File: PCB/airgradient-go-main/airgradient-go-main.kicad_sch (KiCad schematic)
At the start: 155 parts, among them CN1 SM02B-SRSS-TB (LF)(SN), CN2 BM05B-SRSS-TB(LF)(SN), CN3 BM05B-SRSS-TB(LF)(SN), CN4 HCZZ0039-4, Q1 SIA445EDJ-T1-GE3, Q2 ZVN4106FTA_C508255, Q3 SS8050-G, Q4 SI1308EDL, SW1 TS-1091C-A1B3-D2, SW2 TS-1091C-A1B3-D2, U1 W25N512GVEIG, U10 TMUX121NKGR_C22428404, U11 LIS2DH12TR, U12 HYG-8503A, U13 SHT4x, U14 ZDSD512MLGEAG, U15 DPS368XTSA1, U16 TAU1113, U17 S12, U18 TCA9536DTMR, U2 TPS63802DLAR, U3 BQ25628RYKR, U4 ESP32-C5-MINI-1, U5 TPL5010DDCR, U7 TPS7A0228DQNR, U8 BQ27427YZFR, U9 SGP41-D-R4

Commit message: Import v2.0 development state from Bitbucket branch v2.0
Overlay of the v2.0 design work onto the restructured PCB/ layout:
- airgradient-go-main v2.0 WIP: 186 footprints, microSD, PS1-CO,
  Birdy schematic review fixes; adds v2.0 BOM CSVs
- touch-pad v2.0: T1-T3 pads wired to touch controller CS channels,
  +3.1V rail renamed to VCC
- scd4x-module: minor updates
- libraries: new parts (SPL07-003, BM05B-SRSS-TB, PS1-CO, battery
  holder, ESP32-C5 models) and updated footprints; all library and
  3D model references normalized to ${KIPRJMOD}-relative paths
- led_pcb board was dropped in v2.0 (never migrated)

Known open items carried over from review: U14 VDD_IO not yet
connected to the 3.1V rail; U19 (LM66200) still fitted.
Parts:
- removed ANT1: GPS1003, easyeda2kicad:ANT-SMD_L10.0-W3.0, symbol easyeda2kicad:GPS1003
- removed C26, C38: 1uF/50V, easyeda2kicad:C0402, symbol easyeda2kicad:CC0402KRX5R9BB105
- removed C28: 2.2uF/16V, easyeda2kicad:C0402, symbol easyeda2kicad:CL05A225KO5NQNC
- removed CN1: SM02B-SRSS-TB (LF)(SN), easyeda2kicad:CONN-SMD_2P-P1.00_SM02B-SRSS-TB-LF-SN, symbol easyeda2kicad:SM02B-SRSS-TB(LF)(SN)
- removed CN2, CN3: BM05B-SRSS-TB(LF)(SN), easyeda2kicad:CONN-SMD-5P-P1.00_BM05B-SRSS-TB-LF-SN, symbol easyeda2kicad:BM05B-SRSS-TB(LF)(SN)
- removed CN4: HCZZ0039-4, easyeda2kicad:CONN-SMD_HCZZ0039-4, symbol easyeda2kicad:HCZZ0039-4
- removed D4, D5, D6, D7: CUS10S30,H3F, easyeda2kicad:SOD-323_L1.8-W1.3-LS2.5-RD, symbol easyeda2kicad:CUS10S30,H3F
- removed R28, R30: 10K, easyeda2kicad:R0402, symbol easyeda2kicad:MR04X1002FTL
- removed R29: 0R, easyeda2kicad:R0402, symbol easyeda2kicad:RC0402FR-070RL
- removed TP11: V1.8, TestPoint:TestPoint_Pad_D1.0mm, symbol Connector:TestPoint
- removed TP9: EN_PM1, TestPoint:TestPoint_Pad_D1.0mm, symbol Connector:TestPoint
- removed U15: DPS368XTSA1, easyeda2kicad:LGA-8_L2.5-W2.0-P0.65-TR_DPS368, symbol easyeda2kicad:DPS368XTSA1
- removed U18: TCA9536DTMR, easyeda2kicad:X2SON-8_L1.4-W0.8-P0.50-BL, symbol easyeda2kicad:TCA9536DTMR
- removed U8: BQ27427YZFR, easyeda2kicad:DSBGA-9_L1.6-W1.6-R3-C3-P0.50-TL, symbol easyeda2kicad:BQ27427YZFR
- added AE1: Antenna, AG-lib-oaf:CA-G01, symbol Device:Antenna
- added BT1: Battery_Cell, AG-lib-oaf:AGGO-battery, symbol Device:Battery_Cell
- added C10, C13, C16, C5, C7, C70, C71, C72, C73, C74, C9: 0.1uF/25V, Capacitor_SMD:C_0402_1005Metric, symbol Device:C
- added C26, C42, C66, C67, C68: 1uF/50V, Capacitor_SMD:C_0402_1005Metric, symbol Device:C
- added C27: 0.47uF/25V, Capacitor_SMD:C_0402_1005Metric, symbol Device:C
- added C69: 0.1uF/16V, Capacitor_SMD:C_0402_1005Metric, symbol Device:C
- added CN3, CN4, CN5: SM05B-SRSS-TB (LF)(SN), easyeda2kicad-oaf:CONN-SMD_SM05B-SRSS-TB-LF-SN, symbol easyeda2kicad-oaf:SM05B-SRSS-TB(LF)(SN)
- added LED1, LED2, LED3, LED4: TJ-S1608SW6TDSLCCYRGB-A5, easyeda2kicad-oaf:LED-ARRAY-SMD_4P-L1.6-W0.8-BL-FD, symbol easyeda2kicad-oaf:TJ-S1608SW6TDSLCCYRGB-A5
- added NT1: NetTie_2, NetTie:NetTie-2_SMD_Pad0.5mm, symbol Device:NetTie_2
- added NTC2: NCP15XH103F03RC, easyeda2kicad-oaf:R0402, symbol easyeda2kicad-oaf:NCP15XH103F03RC
- added Q3: CSD83325L, easyeda2kicad-oaf:PICOSTAR-6_L2.2-W1.1-R2-C3-P0.65-BL, symbol easyeda2kicad-oaf:CSD83325L
- added R12, R5: 200R, Resistor_SMD:R_0402_1005Metric, symbol Device:R
- added R13: 2K, Resistor_SMD:R_0402_1005Metric, symbol Device:R
- added R17, R20: 1K, Resistor_SMD:R_0402_1005Metric, symbol Device:R
- added R35: 470mR, Resistor_SMD:R_0805_2012Metric, symbol Device:R
- added R38, R46, R59: 100K, Resistor_SMD:R_0402_1005Metric, symbol Device:R
- added R47, R48: 0R, Resistor_SMD:R_0402_1005Metric, symbol Device:R
- added R49: 5.1K, Resistor_SMD:R_0402_1005Metric, symbol Device:R
- added R50, R51, R52, R53: 22R, Resistor_SMD:R_0402_1005Metric, symbol Device:R
- added R54, R55, R56, R57, R58: 10K, Resistor_SMD:R_0402_1005Metric, symbol Device:R
- added R6, R9: 10R, Resistor_SMD:R_0402_1005Metric, symbol Device:R
- added R8: 5mR 1%/1W, Resistor_SMD:R_1206_3216Metric, symbol Device:R
- added TF1: TF-CARD XG8P H1.5, easyeda2kicad-oaf:TF-SMD_TF-CARD-XG8P-H1.5, symbol easyeda2kicad-oaf:TF-CARDXG8PH1.5
- added TP16, TP17: VBUS, TestPoint:TestPoint_Pad_D1.0mm, symbol Connector:TestPoint
- added U11: PS1-CO-SMOKE-10k, AG-lib-oaf:PS1-CO-SMOKE-10k, symbol AG_lib-oaf:PS1-CO-SMOKE-10k
- added U13: SPL07-003, easyeda2kicad-oaf:LGA-10_L2.0-W2.0-P0.50-BL, symbol easyeda2kicad-oaf:SPL07-003
- added U17: TCA6408ARGT, Package_DFN_QFN:VQFN-16-1EP_3x3mm_P0.5mm_EP1.45x1.45mm, symbol Interface_Expansion:TCA6408ARGT
- added U19: LM66200DRLR, easyeda2kicad-oaf:SOT-583-8_L2.1-W1.2-P0.50-LS1.6-BL, symbol easyeda2kicad-oaf:LM66200DRLR
- added U20: LP5036, Package_DFN_QFN:VQFN-46-1EP_5x6mm_P0.4mm_EP2.8x3.8mm, symbol Driver_LED:LP5036
- added U3: BQ27742YZFR-G1, easyeda2kicad-oaf:DSBGA-15_L2.6-W2.0-R5-C3-P0.50-BL, symbol easyeda2kicad-oaf:BQ27742YZFR-G1
- C1: footprint easyeda2kicad:C0402 -> Capacitor_SMD:C_0402_1005Metric; symbol easyeda2kicad:CL05A104KA5NNNC -> Device:C
- C11: renamed from C4; footprint easyeda2kicad:C0603 -> Capacitor_SMD:C_0603_1608Metric; symbol easyeda2kicad:CL10A106MA8NRNC -> Device:C
- C12: renamed from C5; footprint easyeda2kicad:C0805 -> Capacitor_SMD:C_0805_2012Metric; symbol easyeda2kicad:CL21A226MAYNNNE -> Device:C
- C14: renamed from C33; footprint easyeda2kicad:C0402 -> Capacitor_SMD:C_0402_1005Metric; symbol easyeda2kicad:CL05A104KA5NNNC -> Device:C; now not fitted; now left out of the parts list
- C15: renamed from C6; footprint easyeda2kicad:C0402 -> Capacitor_SMD:C_0402_1005Metric; symbol easyeda2kicad:CL05A104KA5NNNC -> Device:C
- C17: renamed from C7; value 10uF/10V -> 0.1uF/10V; footprint easyeda2kicad:C0402 -> Capacitor_SMD:C_0402_1005Metric; symbol easyeda2kicad:CL05A106MP5NUNC_C315248 -> Device:C
- C18: renamed from C48; footprint easyeda2kicad:C0402 -> Capacitor_SMD:C_0402_1005Metric; symbol easyeda2kicad:CC0402KRX5R9BB105 -> Device:C; now not fitted; now left out of the parts list
- C19: renamed from C9; footprint easyeda2kicad:C0402 -> Capacitor_SMD:C_0402_1005Metric; symbol easyeda2kicad:CC0402KRX5R9BB105 -> Device:C
- C2: footprint easyeda2kicad:C0402 -> Capacitor_SMD:C_0402_1005Metric; symbol easyeda2kicad:0402B473K250NT -> Device:C
- C20: footprint easyeda2kicad:C1206 -> Capacitor_SMD:C_1206_3216Metric; symbol easyeda2kicad:GRM31CR61E476ME44L -> Device:C
- C21: renamed from C10; value 10uF/10V -> 22uF/10V; footprint easyeda2kicad:C0402 -> Capacitor_SMD:C_0402_1005Metric; symbol easyeda2kicad:CL05A106MP5NUNC_C315248 -> Device:C
- C22: renamed from C11; footprint easyeda2kicad:C0603 -> Capacitor_SMD:C_0603_1608Metric; symbol easyeda2kicad:CL10A106MA8NRNC -> Device:C
- C23: renamed from C24; now left out of the parts list
- C24: renamed from C14; footprint easyeda2kicad:C0402 -> Capacitor_SMD:C_0402_1005Metric; symbol easyeda2kicad:CL05A104KA5NNNC -> Device:C
- C25: renamed from C18; now left out of the parts list
- C28: renamed from C29; footprint easyeda2kicad:C0402 -> Capacitor_SMD:C_0402_1005Metric; symbol easyeda2kicad:CL05A104KA5NNNC -> Device:C
- C29: renamed from C27; footprint easyeda2kicad:C0402 -> Capacitor_SMD:C_0402_1005Metric; symbol easyeda2kicad:CC0402KRX5R9BB105 -> Device:C
- C3: renamed from C12; footprint easyeda2kicad:C0402 -> Capacitor_SMD:C_0402_1005Metric; symbol easyeda2kicad:CL05A104KA5NNNC -> Device:C
- C30: renamed from C19; footprint easyeda2kicad:C0402 -> Capacitor_SMD:C_0402_1005Metric; symbol easyeda2kicad:CC0402KRX5R9BB105 -> Device:C
- C31: renamed from C21; footprint easyeda2kicad:C0402 -> Capacitor_SMD:C_0402_1005Metric; symbol easyeda2kicad:CC0402KRX7R9BB102 -> Device:C; now left out of the parts list
- C32: renamed from C22; footprint easyeda2kicad:C0402 -> Capacitor_SMD:C_0402_1005Metric; symbol easyeda2kicad:CC0402KRX7R9BB102 -> Device:C; now left out of the parts list
- C33: renamed from C23; footprint easyeda2kicad:C0603 -> Capacitor_SMD:C_0603_1608Metric; symbol easyeda2kicad:0603B501K500NT -> Device:C
- C34: renamed from C25; footprint easyeda2kicad:C0402 -> Capacitor_SMD:C_0402_1005Metric; symbol easyeda2kicad:CC0402KRX7R6BB103 -> Device:C; now left out of the parts list
- C35: renamed from C31; footprint easyeda2kicad:C0402 -> Capacitor_SMD:C_0402_1005Metric; symbol easyeda2kicad:CC0402KRX5R9BB105 -> Device:C
- C36: renamed from C8; footprint easyeda2kicad:C0805 -> Capacitor_SMD:C_0805_2012Metric; symbol easyeda2kicad:CL21A226MAYNNNE -> Device:C
- C37: renamed from C13; footprint easyeda2kicad:C0805 -> Capacitor_SMD:C_0805_2012Metric; symbol easyeda2kicad:CL21A226MAYNNNE -> Device:C
- C38: renamed from C17; footprint easyeda2kicad:C0805 -> Capacitor_SMD:C_0805_2012Metric; symbol easyeda2kicad:CL21A226MAYNNNE -> Device:C
- C39: renamed from C49; footprint easyeda2kicad:C0402 -> Capacitor_SMD:C_0402_1005Metric; symbol easyeda2kicad:CL05A104KA5NNNC -> Device:C
- C4: renamed from C3; footprint easyeda2kicad:C0603 -> Capacitor_SMD:C_0603_1608Metric; symbol easyeda2kicad:CL10A106MA8NRNC -> Device:C
- C40: renamed from C52; footprint easyeda2kicad:C0402 -> Capacitor_SMD:C_0402_1005Metric; symbol easyeda2kicad:CC0402KRX5R9BB105 -> Device:C
- C41: renamed from C34; footprint easyeda2kicad:C0402 -> Capacitor_SMD:C_0402_1005Metric; symbol easyeda2kicad:CC0402KRX5R9BB105 -> Device:C
- C43: renamed from C35; footprint easyeda2kicad:C0402 -> Capacitor_SMD:C_0402_1005Metric; symbol easyeda2kicad:CC0402KRX5R9BB105 -> Device:C
- C44: renamed from C39; footprint easyeda2kicad:C0402 -> Capacitor_SMD:C_0402_1005Metric; symbol easyeda2kicad:CC0402KRX5R9BB105 -> Device:C
- C45: renamed from C30; footprint easyeda2kicad:C0402 -> Capacitor_SMD:C_0402_1005Metric; symbol easyeda2kicad:CGA0402X5R475M250GT -> Device:C
- C46: renamed from C41; footprint easyeda2kicad:C0402 -> Capacitor_SMD:C_0402_1005Metric; symbol easyeda2kicad:CC0402KRX5R9BB105 -> Device:C
- C47: renamed from C56; footprint easyeda2kicad:C0402 -> Capacitor_SMD:C_0402_1005Metric; symbol easyeda2kicad:CC0402KRX5R9BB105 -> Device:C
- C48: renamed from C32; footprint easyeda2kicad:C0402 -> Capacitor_SMD:C_0402_1005Metric; symbol easyeda2kicad:CGA0402X5R475M250GT -> Device:C
- C49: renamed from C40; footprint easyeda2kicad:C0402 -> Capacitor_SMD:C_0402_1005Metric; symbol easyeda2kicad:CC0402KRX5R9BB105 -> Device:C
- C50: renamed from C57; footprint easyeda2kicad:C0402 -> Capacitor_SMD:C_0402_1005Metric; symbol easyeda2kicad:CC0402KRX5R9BB105 -> Device:C
- C51: renamed from C42; footprint easyeda2kicad:C0402 -> Capacitor_SMD:C_0402_1005Metric; symbol easyeda2kicad:CC0402KRX5R9BB105 -> Device:C
- C52: renamed from C58; footprint easyeda2kicad:C0402 -> Capacitor_SMD:C_0402_1005Metric; symbol easyeda2kicad:CL05A104KA5NNNC -> Device:C
- C53: renamed from C43; footprint easyeda2kicad:C0402 -> Capacitor_SMD:C_0402_1005Metric; symbol easyeda2kicad:CC0402KRX5R9BB105 -> Device:C
- C54: renamed from C36; footprint easyeda2kicad:C0402 -> Capacitor_SMD:C_0402_1005Metric; symbol easyeda2kicad:CC0402KRX5R9BB105 -> Device:C
- C55: renamed from C37; footprint easyeda2kicad:C0402 -> Capacitor_SMD:C_0402_1005Metric; symbol easyeda2kicad:CC0402KRX5R9BB105 -> Device:C
- C56: renamed from C50; footprint easyeda2kicad:C0402 -> Capacitor_SMD:C_0402_1005Metric; symbol easyeda2kicad:CL05A104KA5NNNC -> Device:C
- C57: renamed from C60; footprint easyeda2kicad:C0402 -> Capacitor_SMD:C_0402_1005Metric; symbol easyeda2kicad:CL05A104KA5NNNC -> Device:C
- C58: renamed from C45; footprint easyeda2kicad:C0402 -> Capacitor_SMD:C_0402_1005Metric; symbol easyeda2kicad:CC0402KRX5R9BB105 -> Device:C
- C59: renamed from C46; footprint easyeda2kicad:C0402 -> Capacitor_SMD:C_0402_1005Metric; symbol easyeda2kicad:CL05A104KA5NNNC -> Device:C
- C6: renamed from C15; footprint easyeda2kicad:C0603 -> Capacitor_SMD:C_0603_1608Metric; symbol easyeda2kicad:CL10A106MA8NRNC -> Device:C
- C60: renamed from C53; footprint easyeda2kicad:C0603 -> Capacitor_SMD:C_0603_1608Metric; symbol easyeda2kicad:CL10A106MA8NRNC -> Device:C
- C61: renamed from C47; now left out of the parts list
- C62: renamed from C51; now left out of the parts list
- C63: renamed from C54; footprint easyeda2kicad:C0402 -> Capacitor_SMD:C_0402_1005Metric; symbol easyeda2kicad:CL05A104KA5NNNC -> Device:C
- C64: renamed from C55; footprint easyeda2kicad:C0402 -> Capacitor_SMD:C_0402_1005Metric; symbol easyeda2kicad:CC0402KRX5R9BB105 -> Device:C
- C65: renamed from C59; footprint easyeda2kicad:C0603 -> Capacitor_SMD:C_0603_1608Metric; symbol easyeda2kicad:CL10A106MA8NRNC -> Device:C
- C8: renamed from C16; footprint easyeda2kicad:C0402 -> Capacitor_SMD:C_0402_1005Metric; symbol easyeda2kicad:CGA0402X5R475M250GT -> Device:C
- D3: renamed from D1; footprint easyeda2kicad:SOD-882_L1.0-W0.6-RD -> easyeda2kicad-oaf:SOD-882_L1.0-W0.6-RD; symbol easyeda2kicad:PMEG3005EL,315 -> easyeda2kicad-oaf:PMEG3005EL,315
- D4: renamed from D2; footprint easyeda2kicad:SOD-882_L1.0-W0.6-RD -> easyeda2kicad-oaf:SOD-882_L1.0-W0.6-RD; symbol easyeda2kicad:PMEG3005EL,315 -> easyeda2kicad-oaf:PMEG3005EL,315
- D5: renamed from D3; footprint easyeda2kicad:SOD-882_L1.0-W0.6-RD -> easyeda2kicad-oaf:SOD-882_L1.0-W0.6-RD; symbol easyeda2kicad:PMEG3005EL,315 -> easyeda2kicad-oaf:PMEG3005EL,315
- F1: footprint easyeda2kicad:F1206 -> easyeda2kicad-oaf:F1206; symbol easyeda2kicad:BSMD1206-075-6V -> easyeda2kicad-oaf:BSMD1206-075-6V
- FPC1: footprint easyeda2kicad:FPC-SMD_FPC-0.5-24P-LTH2.0 -> easyeda2kicad-oaf:FPC-SMD_FPC-0.5-24P-LTH2.0; symbol easyeda2kicad:FPC0.5-24PLTH2.0 -> easyeda2kicad-oaf:FPC0.5-24PLTH2.0
- L1: footprint easyeda2kicad:IND-SMD_L2.5-W2.0 -> easyeda2kicad-oaf:IND-SMD_L2.5-W2.0; symbol easyeda2kicad:252012CDMCDDS-1R0MC -> easyeda2kicad-oaf:252012CDMCDDS-1R0MC
- L2: footprint easyeda2kicad:IND-SMD_L4.0-W4.0_XGL4020 -> easyeda2kicad-oaf:IND-SMD_L4.0-W4.0_XGL4020; symbol easyeda2kicad:XGL4020-471MEC -> easyeda2kicad-oaf:XGL4020-471MEC
- L3: footprint easyeda2kicad:L0805 -> easyeda2kicad-oaf:L0805; symbol easyeda2kicad:XRTC201210S100MBCA -> easyeda2kicad-oaf:XRTC201210S100MBCA
- NTC1: footprint easyeda2kicad:R0805 -> easyeda2kicad-oaf:R0805; symbol easyeda2kicad:KNTC0805_10KF3950 -> easyeda2kicad-oaf:KNTC0805_10KF3950
- Q1: footprint easyeda2kicad:SC-70-6L_L2.0-W2.0-P0.65-BL -> easyeda2kicad-oaf:SC-70-6L_L2.0-W2.0-P0.65-BL; symbol easyeda2kicad:SIA445EDJ-T1-GE3 -> easyeda2kicad-oaf:SIA445EDJ-T1-GE3
- Q2: footprint easyeda2kicad:SOT-23-3_L2.9-W1.3-P1.90-LS2.4-BR -> easyeda2kicad-oaf:SOT-23-3_L2.9-W1.3-P1.90-LS2.4-BR; symbol easyeda2kicad:ZVN4106FTA_C508255 -> easyeda2kicad-oaf:ZVN4106FTA_C508255
- Q4: renamed from Q3; footprint easyeda2kicad:SOT-23-3_L2.9-W1.3-P1.90-LS2.4-BR -> easyeda2kicad-oaf:SOT-23-3_L2.9-W1.3-P1.90-LS2.4-BR; symbol easyeda2kicad:SS8050-G -> easyeda2kicad-oaf:SS8050-G
- Q5: renamed from Q4; footprint easyeda2kicad:SOT-323-3_L2.0-W1.3-P1.30-LS2.1-BR -> easyeda2kicad-oaf:SOT-323-3_L2.0-W1.3-P1.30-LS2.1-BR; symbol easyeda2kicad:SI1308EDL -> easyeda2kicad-oaf:SI1308EDL
- R1: footprint easyeda2kicad:R0402 -> Resistor_SMD:R_0402_1005Metric; symbol easyeda2kicad:RC0402FR-07100KL -> Device:R
- R10: renamed from R14; footprint easyeda2kicad:R0402 -> Resistor_SMD:R_0402_1005Metric; symbol easyeda2kicad:MR04X1002FTL -> Device:R
- R11: renamed from R9; footprint easyeda2kicad:R0402 -> Resistor_SMD:R_0402_1005Metric; symbol easyeda2kicad:RC0402FR-075K1L -> Device:R
- R14: renamed from R10; footprint easyeda2kicad:R0402 -> Resistor_SMD:R_0402_1005Metric; symbol easyeda2kicad:MR04X1002FTL -> Device:R
- R15: renamed from R17; footprint easyeda2kicad:R0402 -> Resistor_SMD:R_0402_1005Metric; symbol easyeda2kicad:0402WGF1502TCE -> Device:R
- R16: renamed from R18; footprint easyeda2kicad:R0402 -> Resistor_SMD:R_0402_1005Metric; symbol easyeda2kicad:RC0402FR-0720KL -> Device:R
- R18: renamed from R11; footprint easyeda2kicad:R0402 -> Resistor_SMD:R_0402_1005Metric; symbol easyeda2kicad:RC0402FR-074K12L -> Device:R
- R19: renamed from R12; footprint easyeda2kicad:R0402 -> Resistor_SMD:R_0402_1005Metric; symbol easyeda2kicad:AT0402DRD0717K4L -> Device:R
- R2, R3: footprint easyeda2kicad:R0402 -> Resistor_SMD:R_0402_1005Metric; symbol easyeda2kicad:MR04X1002FTL -> Device:R
- R21: renamed from R13; footprint easyeda2kicad:R0402 -> Resistor_SMD:R_0402_1005Metric; symbol easyeda2kicad:0402WGF2491TCE -> Device:R
- R22: renamed from R4; footprint easyeda2kicad:R0402 -> Resistor_SMD:R_0402_1005Metric; symbol easyeda2kicad:FRC0402F4753TS -> Device:R
- R23: renamed from R38; footprint easyeda2kicad:R0402 -> Resistor_SMD:R_0402_1005Metric; symbol easyeda2kicad:RC0402FR-071KL -> Device:R
- R24: renamed from R6; footprint easyeda2kicad:R0402 -> Resistor_SMD:R_0402_1005Metric; symbol easyeda2kicad:RC0402FR-0791KL -> Device:R
- R25: renamed from R16; footprint easyeda2kicad:R0402 -> Resistor_SMD:R_0402_1005Metric; symbol easyeda2kicad:RC0402FR-0751KL -> Device:R
- R26: renamed from R19; footprint easyeda2kicad:R0402 -> Resistor_SMD:R_0402_1005Metric; symbol easyeda2kicad:MR04X1002FTL -> Device:R
- R27: renamed from R20; footprint easyeda2kicad:R0402 -> Resistor_SMD:R_0402_1005Metric; symbol easyeda2kicad:RC0402FR-0722RL -> Device:R
- R28: renamed from R21; footprint easyeda2kicad:R0402 -> Resistor_SMD:R_0402_1005Metric; symbol easyeda2kicad:RC0402FR-0722RL -> Device:R
- R29: renamed from R8; footprint easyeda2kicad:R0402 -> Resistor_SMD:R_0402_1005Metric; symbol easyeda2kicad:RC0402FR-07100KL -> Device:R
- R30: renamed from R22; footprint easyeda2kicad:R0402 -> Resistor_SMD:R_0402_1005Metric; symbol easyeda2kicad:MR04X1002FTL -> Device:R
- R31: renamed from R23; footprint easyeda2kicad:R0402 -> Resistor_SMD:R_0402_1005Metric; symbol easyeda2kicad:RC0402FR-07100KL -> Device:R
- R32: renamed from R25; value 0R -> 50mR; footprint easyeda2kicad:R0402 -> Resistor_SMD:R_0805_2012Metric; symbol easyeda2kicad:RC0402FR-070RL -> Device:R
- R33: renamed from R24; value 10K -> 100K; footprint easyeda2kicad:R0402 -> Resistor_SMD:R_0402_1005Metric; symbol easyeda2kicad:MR04X1002FTL -> Device:R
- R34: renamed from R36; footprint easyeda2kicad:R0402 -> Resistor_SMD:R_0402_1005Metric; symbol easyeda2kicad:MR04X1002FTL -> Device:R; now not fitted; now left out of the parts list
- R36: renamed from R26; footprint easyeda2kicad:R0402 -> Resistor_SMD:R_0402_1005Metric; symbol easyeda2kicad:MR04X1002FTL -> Device:R
- R37: renamed from R27; footprint easyeda2kicad:R0402 -> Resistor_SMD:R_0402_1005Metric; symbol easyeda2kicad:MR04X1002FTL -> Device:R; now not fitted
- R39: renamed from R31; footprint easyeda2kicad:R0402 -> Resistor_SMD:R_0402_1005Metric; symbol easyeda2kicad:RC0402FR-07100KL -> Device:R
- R4: renamed from R5; footprint easyeda2kicad:R0402 -> Resistor_SMD:R_0402_1005Metric; symbol easyeda2kicad:RC0402FR-07100KL -> Device:R
- R40: renamed from R33; footprint easyeda2kicad:R0402 -> Resistor_SMD:R_0402_1005Metric; symbol easyeda2kicad:RC0402FR-07100KL -> Device:R
- R41: renamed from R35; footprint easyeda2kicad:R0402 -> Resistor_SMD:R_0402_1005Metric; symbol easyeda2kicad:FRC0402F4R70TS -> Device:R
- R42: renamed from R32; footprint easyeda2kicad:R0402 -> Resistor_SMD:R_0402_1005Metric; symbol easyeda2kicad:RC0402FR-071ML -> Device:R
- R43: renamed from R34; footprint easyeda2kicad:R0402 -> Resistor_SMD:R_0402_1005Metric; symbol easyeda2kicad:0402WGF220KTCE -> Device:R
- R44: renamed from R37; value 10K -> 100K; footprint easyeda2kicad:R0402 -> Resistor_SMD:R_0402_1005Metric; symbol easyeda2kicad:MR04X1002FTL -> Device:R
- R45: renamed from R39; footprint easyeda2kicad:R0402 -> Resistor_SMD:R_0402_1005Metric; symbol easyeda2kicad:RC0402FR-070RL -> Device:R
- R7: footprint easyeda2kicad:R0402 -> Resistor_SMD:R_0402_1005Metric; symbol easyeda2kicad:RC0402FR-075K1L -> Device:R
- SW1, SW2: footprint easyeda2kicad:KEY-SMD_3P-L5.5-W3.8-P3.00 -> easyeda2kicad-oaf:KEY-SMD_3P-L5.5-W3.8-P3.00; symbol easyeda2kicad:TS-1091C-A1B3-D2 -> easyeda2kicad-oaf:TS-1091C-A1B3-D2
- TP1: renamed from TP3; now not fitted; now left out of the parts list
- TP10: renamed from TP13; now not fitted; now left out of the parts list
- TP11: renamed from TP14; now not fitted; now left out of the parts list
- TP12: renamed from TP15; now not fitted; now left out of the parts list
- TP13: renamed from TP16; now not fitted; now left out of the parts list
- TP14: renamed from TP17; now not fitted; now left out of the parts list
- TP15: renamed from TP18; now not fitted; now left out of the parts list
- TP2: renamed from TP4; now not fitted; now left out of the parts list
- TP3: renamed from TP1; now not fitted; now left out of the parts list
- TP4: renamed from TP6; now not fitted; now left out of the parts list
- TP5: renamed from TP8; now not fitted; now left out of the parts list
- TP6: renamed from TP7; now not fitted; now left out of the parts list
- TP7: renamed from TP10; now not fitted; now left out of the parts list
- TP8: renamed from TP5; now not fitted; now left out of the parts list
- U1: footprint easyeda2kicad:WSON-8_L8.0-W6.0-P1.27-TL-1 -> easyeda2kicad-oaf:WSON-8_L8.0-W6.0-P1.27-TL-1; symbol easyeda2kicad:W25N512GVEIG -> easyeda2kicad-oaf:W25N512GVEIG
- U10: renamed from U9; footprint Senserion:XDCR_SGP41-D-R4 -> Senserion-oaf:XDCR_SGP41-D-R4; symbol Senserion:SGP41-D-R4 -> Senserion-oaf:SGP41-D-R4; now left out of the parts list
- U12: renamed from U13; now left out of the parts list
- U14: renamed from U11; footprint easyeda2kicad:LGA-12_L2.0-W2.0-P0.50-BL -> easyeda2kicad-oaf:LGA-12_L2.0-W2.0-P0.50-BL; symbol easyeda2kicad:LIS2DH12TR -> easyeda2kicad-oaf:LIS2DH12TR
- U15: renamed from U10; footprint easyeda2kicad:UQFN-10_L1.8-W1.4-P0.40-BL -> easyeda2kicad-oaf:UQFN-10_L1.8-W1.4-P0.40-BL; symbol easyeda2kicad:TMUX121NKGR_C22428404 -> easyeda2kicad-oaf:TMUX121NKGR_C22428404
- U16: renamed from U17; footprint S12:S12 -> S12-oaf:S12; symbol S12:S12 -> S12-oaf:S12; now left out of the parts list
- U18: renamed from U16; footprint RF_GPS:TAU1113 -> RF_GPS-oaf:TAU1113; symbol RF_GPS:TAU1113 -> RF_GPS-oaf:TAU1113
- U2: renamed from U14; footprint easyeda2kicad:LGA-8_L8.0-W6.0-P1.27-TL -> easyeda2kicad-oaf:LGA-8_L8.0-W6.0-P1.27-TL; symbol easyeda2kicad:ZDSD512MLGEAG -> easyeda2kicad-oaf:ZDSD512MLGEAG; now left out of the parts list
- U4: footprint Esparessif:ESP32-C5-MINI-1 -> Esparessif-oaf:ESP32-C5-MINI-1; symbol Espressif:ESP32-C5-MINI-1 -> Espressif-oaf:ESP32-C5-MINI-1; now left out of the parts list
- U5: renamed from U3; footprint easyeda2kicad:WQFN-18_L3.0-W2.5-P0.40-TL -> easyeda2kicad-oaf:WQFN-18_L3.0-W2.5-P0.40-TL; symbol easyeda2kicad:BQ25628RYKR -> easyeda2kicad-oaf:BQ25628RYKR
- U6: renamed from U12; footprint easyeda2kicad:BUZ-SMD_4P-L8.5-W8.5-P8.50-BR -> easyeda2kicad-oaf:BUZ-SMD_4P-L8.5-W8.5-P8.50-BR; symbol easyeda2kicad:HYG-8503A -> easyeda2kicad-oaf:HYG-8503A
- U7: renamed from U5; footprint easyeda2kicad:SOT-23-6_L2.9-W1.6-P0.95-LS2.8-BR -> easyeda2kicad-oaf:SOT-23-6_L2.9-W1.6-P0.95-LS2.8-BR; symbol easyeda2kicad:TPL5010DDCR -> easyeda2kicad-oaf:TPL5010DDCR
- U8: renamed from U2; footprint easyeda2kicad:VSON-10_L3.0-W2.0-P0.50-TL -> easyeda2kicad-oaf:VSON-10_L3.0-W2.0-P0.50-TL; symbol easyeda2kicad:TPS63802DLAR -> easyeda2kicad-oaf:TPS63802DLAR
- U9: renamed from U7; footprint easyeda2kicad:X2SON-4_L1.0-W1.0-P0.65-TL-EP -> easyeda2kicad-oaf:X2SON-4_L1.0-W1.0-P0.65-TL-EP; symbol easyeda2kicad:TPS7A0228DQNR -> easyeda2kicad-oaf:TPS7A0228DQNR
- USB1: footprint easyeda2kicad:USB-C-SMD_G-SWITCH_GT-USB-7010ASV -> easyeda2kicad-oaf:USB-C-SMD_G-SWITCH_GT-USB-7010ASV; symbol easyeda2kicad:GT-USB-7010ASV -> easyeda2kicad-oaf:GT-USB-7010ASV
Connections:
- net +3.1V: now also C42.2, C69.2, C70.2, C71.2, CN4.1, CN5.5, LED1.1 (+), LED2.1 (+), LED3.1 (+), LED4.1 (+), R38.2, R47.1, R54.2, R55.2, R56.2, R57.2, R58.2, R59.2, TF1.4 (VDD), U13.1 (VDDIO), U13.10 (VDD), U17.14 (V_{CCP}), U17.15 (V_{CCI}), U20.39 (ADDR1), U20.40 (VCC), U20.43 (EN); no longer R29.1, U14.10 (VDD_IO), U14.2 (CS)
- net +5V: now also CN3.1
- net ACC_INT: now also U17.8 (P5); no longer U4.7 (IO3)
- net EN_PM1: now also R38.1, U17.3 (P1); no longer R37.1, U4.34 (IO26)
- net GND: now also C42.1, C66.1, C67.1, C68.1, C69.1, C70.1, C71.1, C74.1, CN3.4, CN3.5, CN3.6, CN3.7, CN4.5, CN4.6, CN4.7, CN5.1, CN5.6, CN5.7, NT1.2, R48.1, R49.1, TF1.10 (GND), TF1.11 (GND), TF1.12 (GND), TF1.6 (VSS), TF1.9 (GND), U13.3 (GND), U13.8 (GND), U13.9 (GND), U17.16 (ADDR), U17.17 (EPAD), U17.6 (GND), U19.1 (GND), U19.4 (~{ON}), U19.5 (GND), U20.37 (GND), U20.46 (GND), U20.47 (GND)
- net INT: now also CN4.4, U17.7 (P4); no longer U4.17 (IO1)
- net MISO: now also R50.1
- net MOSI: now also R52.2
- net NAND CS: now also U17.4 (P2); no longer U4.8 (IO4)
- net PM_SCL: now also CN3.3
- net PM_SDA: now also CN3.2
- net PRTRG: now also U17.2 (P0)
- net SCL: now also CN4.3, CN5.3, U13.2 (SCL), U17.12 (SCL), U20.42 (SCL), U3.E3 (SCL)
- net SCLK: now also R51.1
- net SDA: now also CN4.2, CN5.4, U13.4 (SDA), U17.13 (SDA), U20.41 (SDA), U3.C3 (SDA)
- net SYS: now also C66.2, U19.6 (VIN2)
- net USB+: now also R28.1; no longer R28.2
- net USB_D+: now also R28.2; no longer R28.1
- net VBUS: now also R35.1, R46.1
- net VDD_BAK: now also C64.2, U18.6 (V_BCKP)
- net ePaper D/C: now also U17.5 (P3); no longer U4.26 (IO15)
- net at C61.1, R45.1: now also AE1.1 (A)
- net at C28.2, R32.1: now also TP17.1, U19.2 (VOUT), U19.7 (VOUT); no longer U8.1 (EN)
- net at C38.2, R32.2, U8.10 (VIN): now also R29.1, U8.1 (EN), TP16.1
- net Load+ renamed Pack+
- net Pack+: now also C72.1, Q3.A2 (S), Q3.C2 (S), R13.1
- net PACK+ renamed BAT+
- net BAT+: now also BT1.1 (+), C10.2, C5.1, R5.1, R6.1, R8.1, R9.1
- new net: R46.2, U19.8 (ST)
- new net: C72.2, C73.1
- new net: C26.2, C27.1, NTC2.1, U3.E1 (REG25)
- new net: C27.2, NTC2.2, U3.E2 (TS)
- new net: R20.1, U3.A3 (DSG)
- new net: Q3.B2 (G), R20.2
- new net: R47.2, R48.2, U20.38 (ADDR0)
- new net: R49.2, U20.44 (IREF)
- new net: C68.2, U20.45 (VCAP)
- new net: C13.1, R9.2, U3.C1 (VPWR)
- new net: C67.2, R35.2, U19.3 (VIN1)
- new net: R54.1, TF1.1 (DAT2)
- new net: R53.1, R55.1, TF1.2 (CD/DAT3)
- new net: R52.1, R56.1, TF1.3 (CMD)
- new net: R51.2, TF1.5 (CLK)
- new net: R50.2, R57.1, TF1.7 (DAT0)
- new net: R58.1, TF1.8 (DAT1)
- new net: C9.1, R6.2, U3.C2 (BAT)
- new net: R17.1, U3.A2 (CHG)
- new net: Q3.B1 (G), R17.2
- new net: C73.2, Q3.A1 (S), Q3.C1 (S), R12.1, R8.2
- new net: C10.1, C7.1, R12.2, U3.A1 (SRP)
- new net: C5.2, C7.2, R5.2, U3.B1 (SRN)
- new net: C74.2, U14.10 (VDD_IO)
- new net: R59.1, U14.2 (CS)
- new net: C16.1, R13.2, U3.B3 (PACKP)
- new net BAT-: BT1.2 (-), C13.2, C16.2, C26.1, C9.2, NT1.1, U3.D1 (VSS)
- new net IO1: U4.17 (IO1)
- new net IO15: U4.26 (IO15)
- new net IO26: R37.1, U4.34 (IO26)
- new net IO3: U4.7 (IO3)
- new net IO4: U4.8 (IO4)
- new net LED_10_B: U20.28 (OUT27)
- new net LED_10_G: U20.29 (OUT28)
- new net LED_10_R: U20.30 (OUT29)
- new net LED_11_B: U20.31 (OUT30)
- new net LED_11_G: U20.32 (OUT31)
- new net LED_11_R: U20.33 (OUT32)
- new net LED_12_B: U20.34 (OUT33)
- new net LED_12_G: U20.35 (OUT34)
- new net LED_12_R: U20.36 (OUT35)
- new net LED_1_B: LED1.2 (-), U20.1 (OUT0)
- new net LED_1_G: LED1.3 (-), U20.2 (OUT1)
- new net LED_1_R: LED1.4 (-), U20.3 (OUT2)
- new net LED_2_B: LED2.2 (-), U20.4 (OUT3)
- new net LED_2_G: LED2.3 (-), U20.5 (OUT4)
- new net LED_2_R: LED2.4 (-), U20.6 (OUT5)
- new net LED_3_B: LED3.2 (-), U20.7 (OUT6)
- new net LED_3_G: LED3.3 (-), U20.8 (OUT7)
- new net LED_3_R: LED3.4 (-), U20.9 (OUT8)
- new net LED_4_B: LED4.2 (-), U20.10 (OUT9)
- new net LED_4_G: LED4.3 (-), U20.11 (OUT10)
- new net LED_4_R: LED4.4 (-), U20.12 (OUT11)
- new net LED_5_B: U20.13 (OUT12)
- new net LED_5_G: U20.14 (OUT13)
- new net LED_5_R: U20.15 (OUT14)
- new net LED_6_B: U20.16 (OUT15)
- new net LED_6_G: U20.17 (OUT16)
- new net LED_6_R: U20.18 (OUT17)
- new net LED_7_B: U20.19 (OUT18)
- new net LED_7_G: U20.20 (OUT19)
- new net LED_7_R: U20.21 (OUT20)
- new net LED_8_B: U20.22 (OUT21)
- new net LED_8_G: U20.23 (OUT22)
- new net LED_8_R: U20.24 (OUT23)
- new net LED_9_B: U20.25 (OUT24)
- new net LED_9_G: U20.26 (OUT25)
- new net LED_9_R: U20.27 (OUT26)
- new net SD_CS: R53.2, U17.9 (P6)
- no-connect marks 30 -> 29
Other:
- note added: "I2C Address: 0x33"
- note added: "Led ring"
- note added: "SD Card"
- note removed: "C20 Change to 47 ro 22 or add more cap"
- moved on the sheet: C23, C25, C61, C62, D3, D4, D5, FPC1, L1, L2, L3, NTC1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

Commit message: Rework main PCB layout: ESP32-C5 placement, routing, and silkscreen
- Move ESP32-C5 module further inward from the board edge and rework affected track routing
- Improve reference designator silkscreen placement
- Restore SD card section (DNP)
- Add OSHW and AirGradient logos and version label
- Move Q5 closer to L3
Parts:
- C42, C71, R50, R51, R52, R53, R54, R55, R56, R57, R58, TF1, U11: now fitted
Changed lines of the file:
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@@
 		(on_board yes)
 		(in_pos_files yes)
-		(dnp yes)
+		(dnp no)
 		(fields_autoplaced yes)
 		(property "Reference" "#PWR0170"
@@
 		(on_board yes)
 		(in_pos_files yes)
-		(dnp yes)
+		(dnp no)
 		(fields_autoplaced yes)
 		(property "Reference" "TF1"
@@
 		(on_board yes)
 		(in_pos_files yes)
-		(dnp yes)
+		(dnp no)
 		(fields_autoplaced yes)
 		(property "Reference" "R57"
@@
 		(on_board yes)
 		(in_pos_files yes)
-		(dnp yes)
+		(dnp no)
 		(fields_autoplaced yes)
 		(property "Reference" "R52"
@@
 		(on_board yes)
 		(in_pos_files yes)
-		(dnp yes)
+		(dnp no)
 		(fields_autoplaced yes)
 		(property "Reference" "C71"
@@
 		(on_board yes)
 		(in_pos_files yes)
-		(dnp yes)
+		(dnp no)
 		(fields_autoplaced yes)
 		(property "Reference" "C42"
@@
 		(on_board yes)
 		(in_pos_files yes)
-		(dnp yes)
+		(dnp no)
 		(fields_autoplaced yes)
 		(property "Reference" "U11"
@@
 		(on_board yes)
 		(in_pos_files yes)
-		(dnp yes)
+		(dnp no)
 		(fields_autoplaced yes)
 		(property "Reference" "R53"
@@
 		(on_board yes)
 		(in_pos_files yes)
-		(dnp yes)
+		(dnp no)
 		(property "Reference" "R51"
 			(at 461.01 278.384 90)
@@
 		(on_board yes)
 		(in_pos_files yes)
-		(dnp yes)
+		(dnp no)
 		(property "Reference" "R50"
 			(at 471.17 283.464 90)
@@
 		(on_board yes)
 		(in_pos_files yes)
-		(dnp yes)
+		(dnp no)
 		(fields_autoplaced yes)
 		(property "Reference" "R56"
@@
 		(on_board yes)
 		(in_pos_files yes)
-		(dnp yes)
+		(dnp no)
 		(fields_autoplaced yes)
 		(property "Reference" "R55"
@@
 		(on_board yes)
 		(in_pos_files yes)
-		(dnp yes)
+		(dnp no)
 		(fields_autoplaced yes)
 		(property "Reference" "R54"
@@
 		(on_board yes)
 		(in_pos_files yes)
-		(dnp yes)
+		(dnp no)
 		(fields_autoplaced yes)
 		(property "Reference" "R58"

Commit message: Schematic: - Change SPI pull-ups R2/R3/R14 from 10K to 100K - Connect C74 decoupling cap to +3.1V rail (was floating)
PCB:
- Narrow the board outline around the temperature sensor area
- Move S12 0.3mm left and rework nearby I2C tracks
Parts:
- R14, R2, R3: value 10K -> 100K
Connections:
- net +3.1V: now also C74.2, U14.10 (VDD_IO)
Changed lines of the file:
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@@
 	)
 	(junction
+		(at 401.32 266.7)
+		(diameter 0)
+		(color 0 0 0 0)
+	)
+	(junction
 		(at 68.58 237.49)
 		(diameter 0)
@@
 			)
 		)
-		(property "Value" "10K"
+		(property "Value" "100K"
 			(at 24.13 128.2699 0)
 			(show_name no)
@@
 	)
 	(symbol
+		(lib_id "power:VDD")
+		(at 401.32 266.7 0)
+		(unit 1)
+		(body_style 1)
+		(exclude_from_sim no)
+		(in_bom yes)
+		(on_board yes)
+		(in_pos_files yes)
+		(dnp no)
+		(fields_autoplaced yes)
+		(property "Reference" "#PWR0167"
+			(at 401.32 270.51 0)
+			(hide yes)
+			(show_name no)
+			(do_not_autoplace no)
+			(effects
+				(font
+					(size 1.27 1.27)
+				)
+			)
+		)
+		(property "Value" "+3.1V"
+			(at 403.86 265.4299 0)
+			(show_name no)
+			(do_not_autoplace no)
+			(effects
+				(font
+					(size 1.27 1.27)
+				)
+				(justify left)
+			)
+		)
+		(property "Footprint" ""
+			(at 401.32 266.7 0)
+			(hide yes)
+			(show_name no)
+			(do_not_autoplace no)
+			(effects
+				(font
+					(size 1.27 1.27)
+				)
+			)
+		)
+		(property "Datasheet" ""
+			(at 401.32 266.7 0)
+			(hide yes)
+			(show_name no)
+			(do_not_autoplace no)
+			(effects
+				(font
+					(size 1.27 1.27)
+				)
+			)
+		)
+		(property "Description" "Power symbol creates a global label with name \"VDD\""
+			(at 401.32 266.7 0)
+			(hide yes)
+			(show_name no)
+			(do_not_autoplace no)
+			(effects
+				(font
+					(size 1.27 1.27)
+				)
+			)
+		)
+		(pin "1"
+		)
+		(instances
+			(project "airgradient-go-main"
+				(path "/63bfc1c7-4623-455a-8f83-dca1d491c7db"
+					(reference "#PWR0167")
+					(unit 1)
+				)
+			)
+		)
+	)
+	(symbol
 		(lib_id "Device:C")
 		(at 321.31 129.54 180)
@@
 			)
 		)
-		(property "Value" "10K"
+		(property "Value" "100K"
 			(at 90.17 128.2699 0)
 			(show_name no)
@@
 			)
 		)
-		(property "Value" "10K"
+		(property "Value" "100K"
 			(at 33.02 128.2699 0)
 			(show_name no)

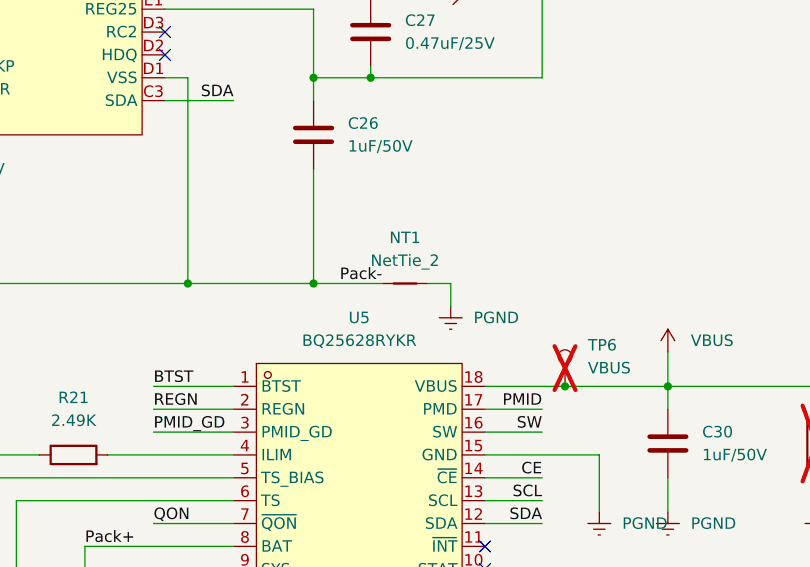
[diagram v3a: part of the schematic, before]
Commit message: Create production files; switch touch pad connector to Hong Cheng
Mainboard:
- Export v2.0 production files (gerbers, BOM, positions) and 3D STEP model
- Add BOM.csv export

Touch pad:
- Change CN1 connector manufacturer from JST to Hong Cheng HCZZ0032-5 (same housing)
- Regenerate production files as v2.0 (BOM now includes full parts list)
- Add Hong Cheng connector symbol, footprint, and 3D model to easyeda2kicad library
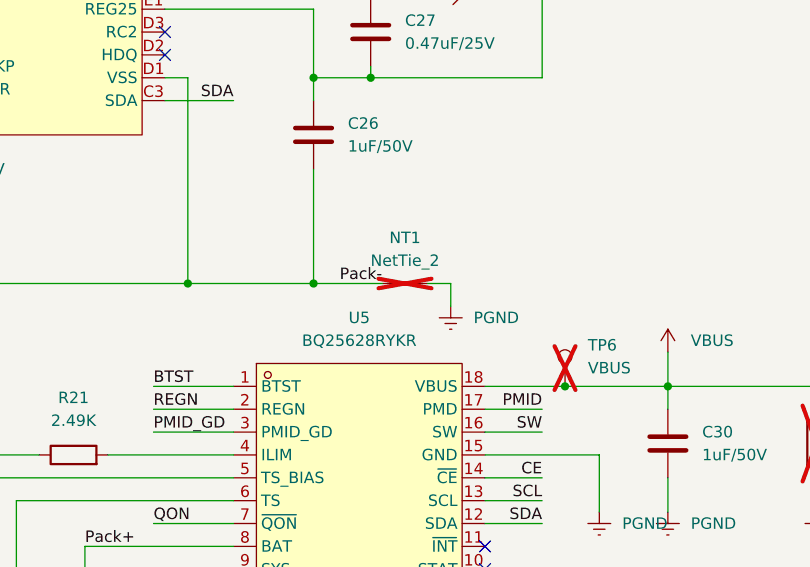
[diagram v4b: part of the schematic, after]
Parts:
- C42, U4: now in the parts list
- NT1: now not fitted
- R37, U11: now left out of the parts list
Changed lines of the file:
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@@
 		(body_style 1)
 		(exclude_from_sim no)
-		(in_bom no)
+		(in_bom yes)
 		(on_board yes)
 		(in_pos_files yes)
@@
 		(body_style 1)
 		(exclude_from_sim no)
-		(in_bom no)
+		(in_bom yes)
 		(on_board yes)
 		(in_pos_files yes)
@@
 		(on_board yes)
 		(in_pos_files yes)
-		(dnp no)
+		(dnp yes)
 		(fields_autoplaced yes)
 		(property "Reference" "NT1"
@@
 		(body_style 1)
 		(exclude_from_sim no)
-		(in_bom yes)
+		(in_bom no)
 		(on_board yes)
 		(in_pos_files yes)
@@
 		(body_style 1)
 		(exclude_from_sim no)
-		(in_bom yes)
+		(in_bom no)
 		(on_board yes)
 		(in_pos_files yes)
